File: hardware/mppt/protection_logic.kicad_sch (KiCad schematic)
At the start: 21 parts, among them IC801 SN74LVC08APWR, IC802 SN74LVC1G04DBVR, IC803 SN74HCS367PWR, IC804 SN74LVC2G32DCUR

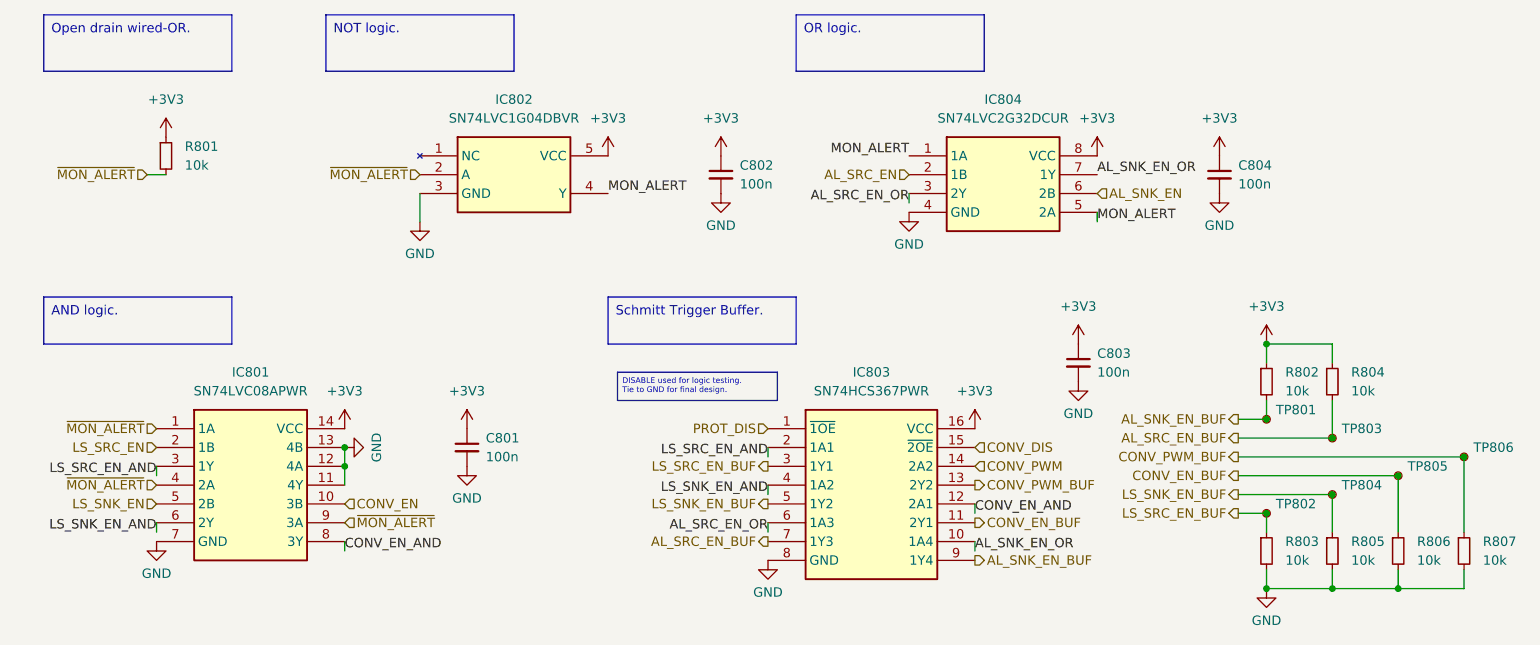
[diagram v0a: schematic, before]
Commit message: run through mppt sch, going through bom
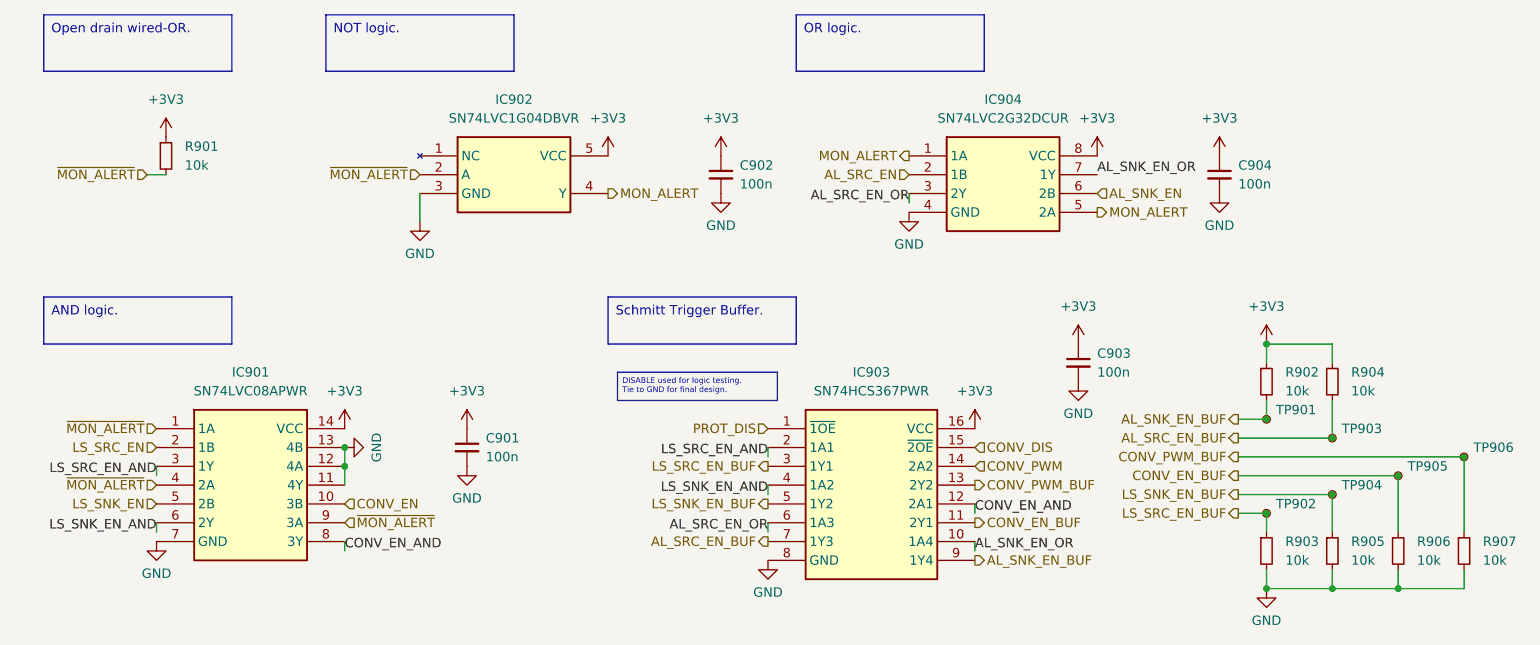
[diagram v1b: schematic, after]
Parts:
- C901: renamed from C801; footprint Capacitor_SMD:C_0805_2012Metric_Pad1.18x1.45mm_HandSolder -> (none); Manufacturer Samsung Microelectronics -> Samsung Electro-Mechanics; Notes 3.3V -> 3.3V Rating
- C902: renamed from C802; footprint Capacitor_SMD:C_0805_2012Metric_Pad1.18x1.45mm_HandSolder -> (none); Manufacturer Samsung Microelectronics -> Samsung Electro-Mechanics; Notes 3.3V -> 3.3V Rating
- C903: renamed from C803; footprint Capacitor_SMD:C_0805_2012Metric_Pad1.18x1.45mm_HandSolder -> (none); Manufacturer Samsung Microelectronics -> Samsung Electro-Mechanics; Notes 3.3V -> 3.3V Rating
- C904: renamed from C804; footprint Capacitor_SMD:C_0805_2012Metric_Pad1.18x1.45mm_HandSolder -> (none); Manufacturer Samsung Microelectronics -> Samsung Electro-Mechanics; Notes 3.3V -> 3.3V Rating
- IC901: renamed from IC801; Distributor Texas Instruments -> (none)
- IC902: renamed from IC802; Distributor Texas Instruments -> (none)
- IC903: renamed from IC803; Distributor Texas Instruments -> (none)
- IC904: renamed from IC804; Distributor Texas Instruments -> (none)
- R901: renamed from R801; footprint Resistor_SMD:R_0805_2012Metric_Pad1.20x1.40mm_HandSolder -> (none)
- R902: renamed from R802; footprint Resistor_SMD:R_0805_2012Metric_Pad1.20x1.40mm_HandSolder -> (none)
- R903: renamed from R803; footprint Resistor_SMD:R_0805_2012Metric_Pad1.20x1.40mm_HandSolder -> (none)
- R904: renamed from R804; footprint Resistor_SMD:R_0805_2012Metric_Pad1.20x1.40mm_HandSolder -> (none)
- R905: renamed from R805; footprint Resistor_SMD:R_0805_2012Metric_Pad1.20x1.40mm_HandSolder -> (none)
- R906: renamed from R806; footprint Resistor_SMD:R_0805_2012Metric_Pad1.20x1.40mm_HandSolder -> (none)
- R907: renamed from R807; footprint Resistor_SMD:R_0805_2012Metric_Pad1.20x1.40mm_HandSolder -> (none)
- TP901: renamed from TP801; footprint TestPoint:TestPoint_Keystone_5000-5004_Miniature -> (none); Manufacturer Keystone Electronics -> (none); P/N 5000 -> (none)
- TP902: renamed from TP802; footprint TestPoint:TestPoint_Keystone_5000-5004_Miniature -> (none); Manufacturer Keystone Electronics -> (none); P/N 5000 -> (none)
- TP903: renamed from TP803; footprint TestPoint:TestPoint_Keystone_5000-5004_Miniature -> (none); Manufacturer Keystone Electronics -> (none); P/N 5000 -> (none)
- TP904: renamed from TP804; footprint TestPoint:TestPoint_Keystone_5000-5004_Miniature -> (none); Manufacturer Keystone Electronics -> (none); P/N 5000 -> (none)
- TP905: renamed from TP805; footprint TestPoint:TestPoint_Keystone_5000-5004_Miniature -> (none); Manufacturer Keystone Electronics -> (none); P/N 5000 -> (none)
- TP906: renamed from TP806; footprint TestPoint:TestPoint_Keystone_5000-5004_Miniature -> (none); Manufacturer Keystone Electronics -> (none); P/N 5000 -> (none)

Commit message: update final missing pieces for sch, moving to bom pop
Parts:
- TP901, TP902, TP903, TP904, TP905, TP906: footprint (none) -> TestPoint:TestPoint_Pad_D1.0mm
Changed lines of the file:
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@@
 			)
 		)
-		(property "Footprint" ""
+		(property "Footprint" "TestPoint:TestPoint_Pad_D1.0mm"
 			(at 208.28 105.41 0)
 			(effects
@@
 			)
 		)
-		(property "Footprint" ""
+		(property "Footprint" "TestPoint:TestPoint_Pad_D1.0mm"
 			(at 226.06 100.33 0)
 			(effects
@@
 			)
 		)
-		(property "Footprint" ""
+		(property "Footprint" "TestPoint:TestPoint_Pad_D1.0mm"
 			(at 234.95 97.79 0)
 			(effects
@@
 			)
 		)
-		(property "Footprint" ""
+		(property "Footprint" "TestPoint:TestPoint_Pad_D1.0mm"
 			(at 208.28 92.71 0)
 			(effects
@@
 			)
 		)
-		(property "Footprint" ""
+		(property "Footprint" "TestPoint:TestPoint_Pad_D1.0mm"
 			(at 217.17 102.87 0)
 			(effects
@@
 			)
 		)
-		(property "Footprint" ""
+		(property "Footprint" "TestPoint:TestPoint_Pad_D1.0mm"
 			(at 217.17 95.25 0)
 			(effects

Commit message: bom consolidated, starting layout
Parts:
- C901, C902, C903, C904: footprint (none) -> Capacitor_SMD:C_0402_1005Metric_Pad0.74x0.62mm_HandSolder; Manufacturer Samsung Electro-Mechanics -> TDK; P/N (none) -> CGA2B3X7R1H104K050BB
- R901, R902, R903, R904, R905, R906, R907: footprint (none) -> Resistor_SMD:R_0603_1608Metric_Pad0.98x0.95mm_HandSolder; P/N (none) -> CRCW060310K0FKEA

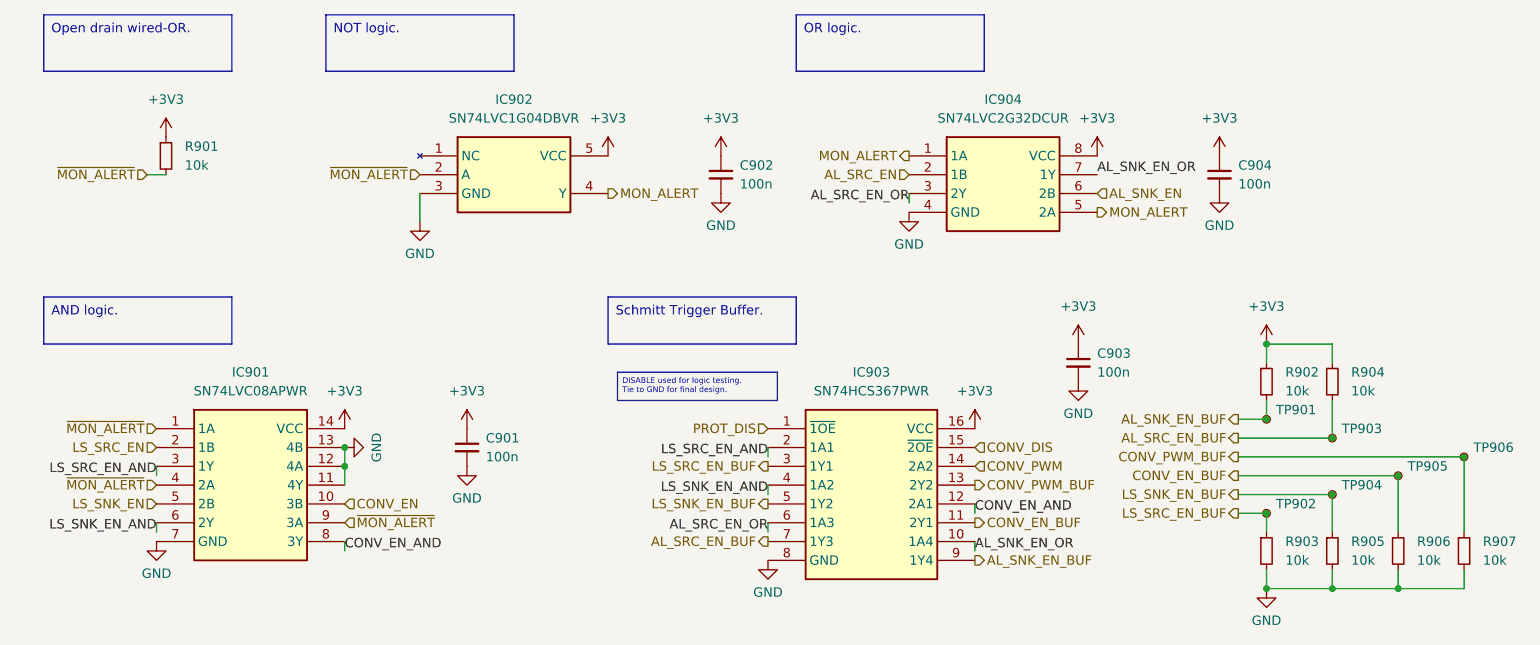
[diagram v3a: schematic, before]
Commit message: PCB variant for power regulation breakout.
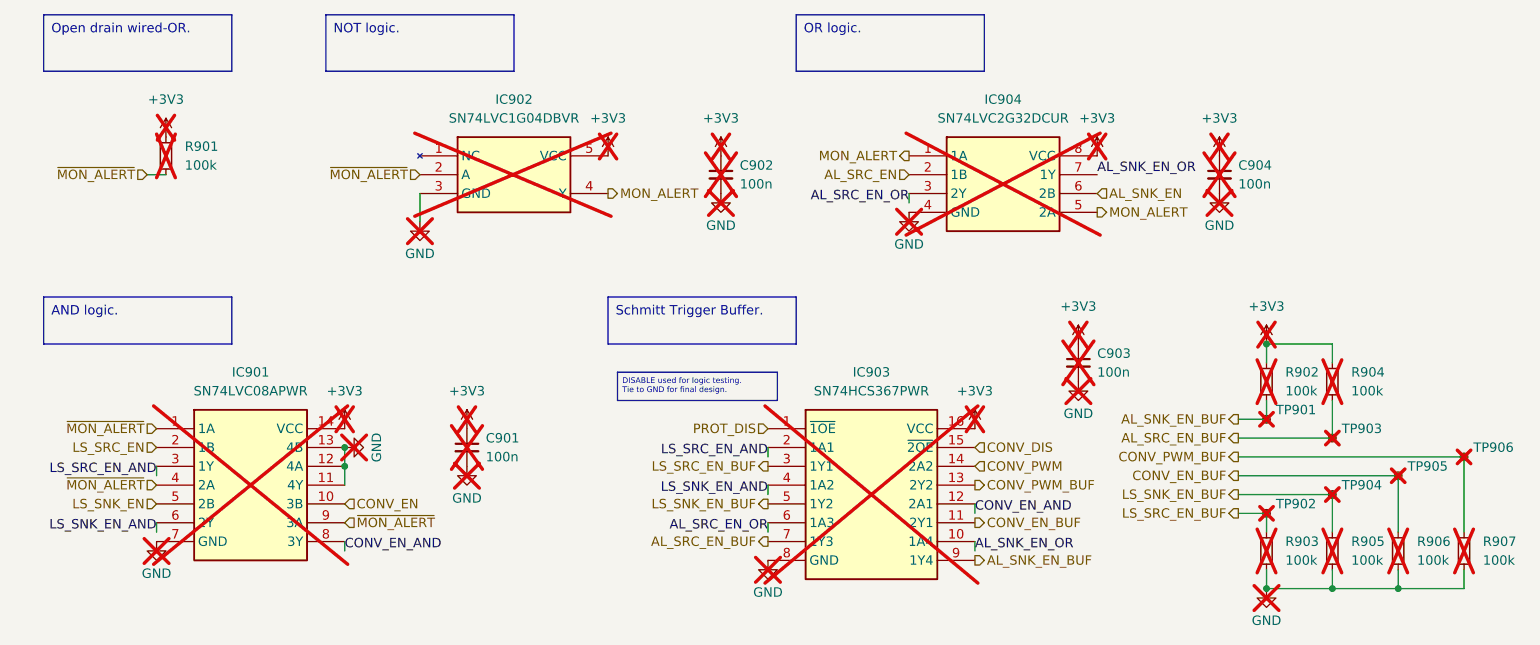
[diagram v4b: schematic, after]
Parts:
- C901, C902, C903, C904, IC901, IC902, IC903, IC904, TP901, TP902, TP903, TP904, TP905, TP906: now not fitted; now left out of the parts list
- R901, R902, R903, R904, R905, R906, R907: value 10k -> 100k; P/N CRCW060310K0FKEA -> CRCW0603100KFKEA; now not fitted; now left out of the parts list

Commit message: converter schematic and layout.
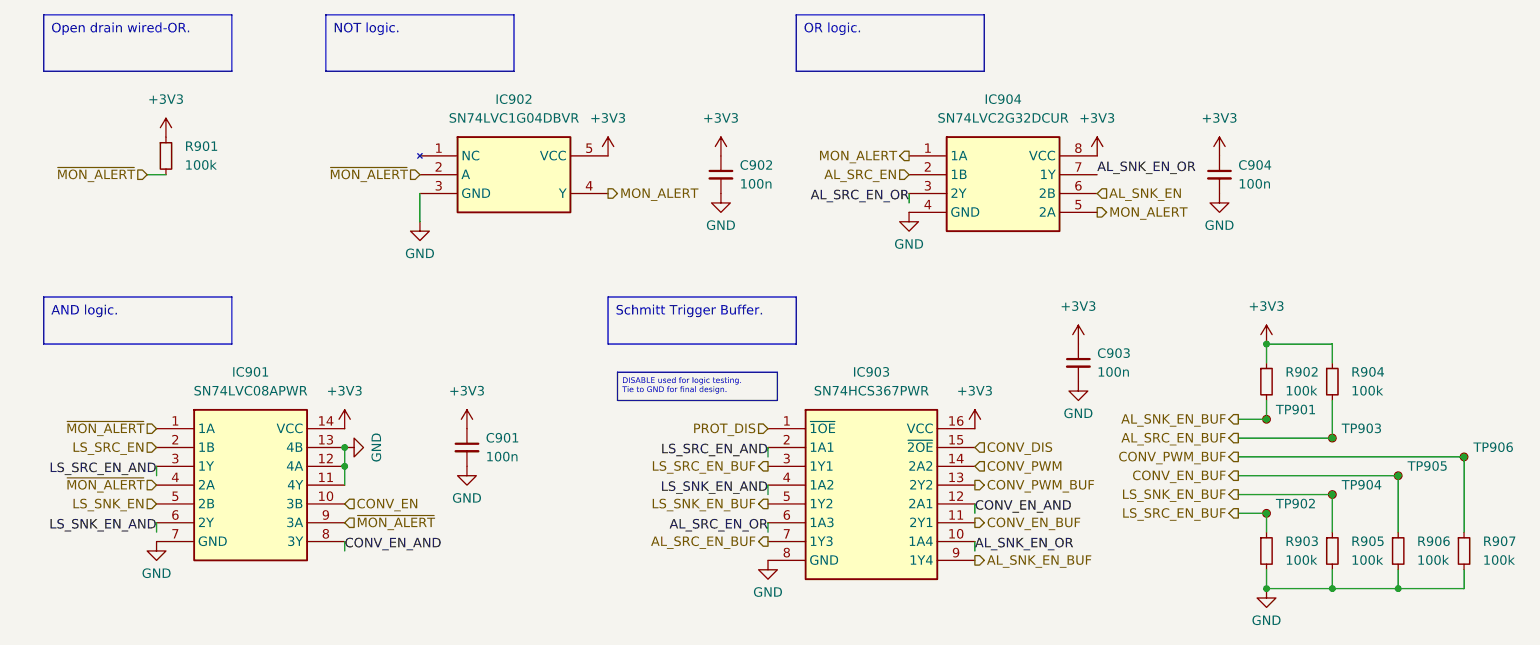
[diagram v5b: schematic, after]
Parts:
- C901, C902, C903, C904, IC901, IC902, IC903, IC904, R901, R902, R903, R904, R905, R906, R907, TP901, TP902, TP903, TP904, TP905, TP906: now fitted; now in the parts list
